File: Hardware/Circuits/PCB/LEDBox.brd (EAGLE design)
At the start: 28 x 28 mm, 19 parts

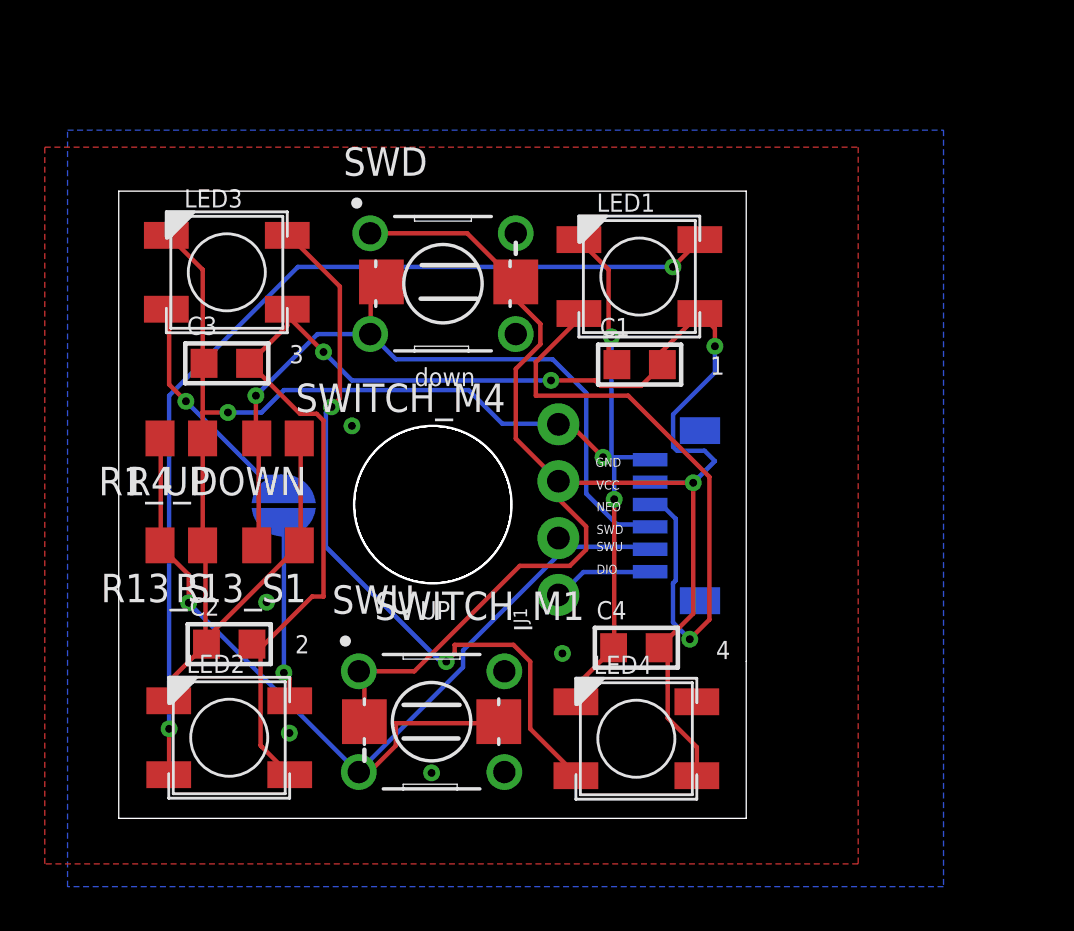
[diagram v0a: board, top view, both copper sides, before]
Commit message: enable Motor
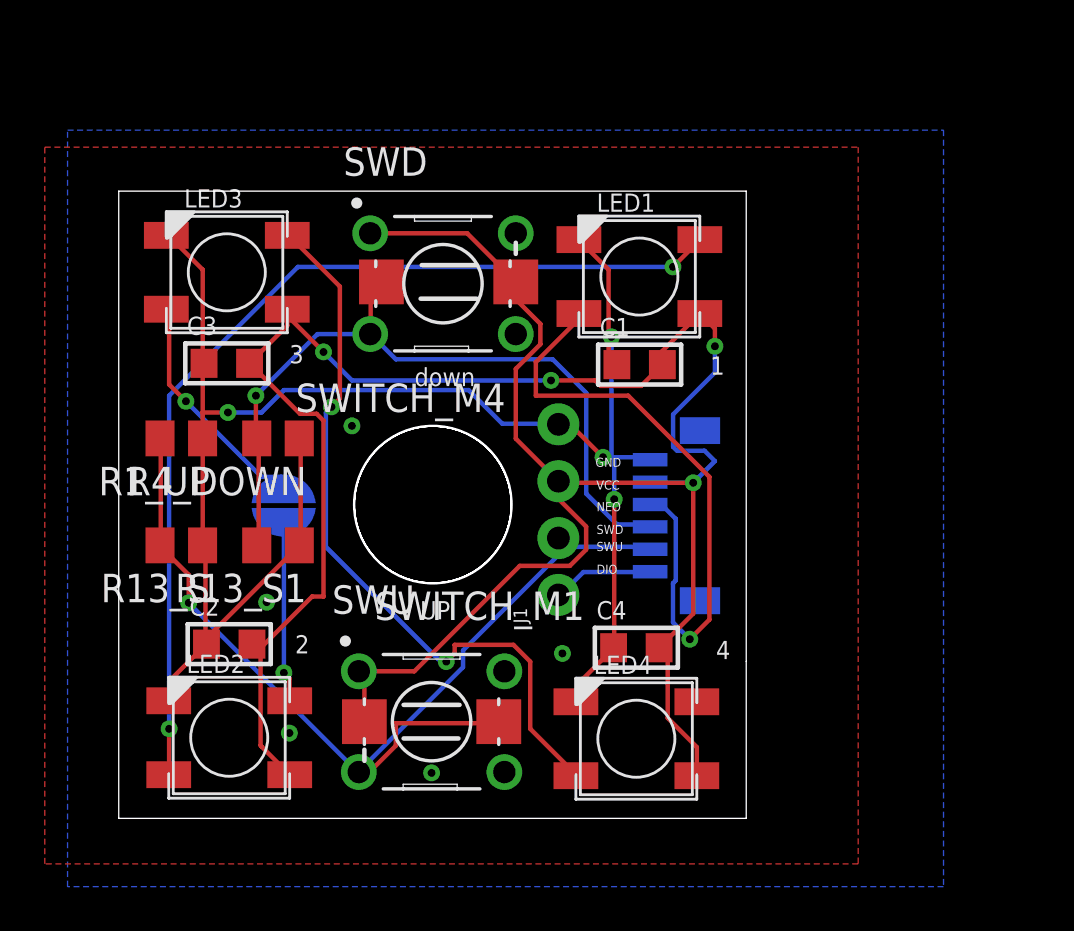
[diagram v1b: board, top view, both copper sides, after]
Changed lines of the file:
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@@
 <?xml version="1.0" encoding="utf-8"?>
 <!DOCTYPE eagle SYSTEM "eagle.dtd">
-<eagle version="9.5.2">
+<eagle version="9.6.2">
 <drawing>
 <settings>
-<setting alwaysvectorfont="no"/>
+<setting alwaysvectorfont="yes"/>
 <setting verticaltext="up"/>
 </settings>
@@
 </layers>
 <board>
-<fusionsync huburn="a.cGVyc29uYWw6dWUyYmFkZWI5" projecturn="a.cGVyc29uYWw6dWUyYmFkZWI5IzIwMTkwNzI5MjA1OTgzMzU2" f3durn="urn:adsk.wipprod:dm.lineage:mkGb1imxSbqdn5AGzfcxTg" pcbguid="4129be0b-5349-4aed-8831-2b5f8f2916f7" lastpulledtime="" lastsyncedchangeguid="7d1ffd36-9ad2-5190-24a6-9f90e3f6ed93"/>
+<fusionsync huburn="a.cGVyc29uYWw6dWUyYmFkZWI5" projecturn="a.cGVyc29uYWw6dWUyYmFkZWI5IzIwMTkwNzI5MjA1OTgzMzU2" f3durn="urn:adsk.wipprod:dm.lineage:mkGb1imxSbqdn5AGzfcxTg" pcbguid="4129be0b-5349-4aed-8831-2b5f8f2916f7" lastpulledtime="2020-11-12T00:39:24Z" lastsyncedchangeguid="3cea0237-b394-707a-1cef-9979548a3917" latestrevisionid="" lastsyncedrevisionid="" lastboardhashguid="3cea0237-b394-707a-1cef-9979548a3917" lastpushedtime="2020-11-12T00:31:10Z" linktopcb3d="false"/>
 <fusionteam huburn="a.cGVyc29uYWw6dWUyYmFkZWI5" projecturn="a.cGVyc29uYWw6dWUyYmFkZWI5IzIwMTkwNzI5MjA1OTgzMzU2" folderUrn="urn:adsk.wipprod:fs.folder:co.fyRBnQNXQZ2K2Ph0YUv8vg" urn="urn:adsk.wipprod:dm.lineage:N41nUebqTaO0nGd6K4BbkA"  versionUrn="urn:adsk.wipprod:fs.file:vf.N41nUebqTaO0nGd6K4BbkA?version=3" camFileUrn="" camFileVersionUrn="" lastpublishedchangeguid="acd2ba34-f1b5-65f4-59b4-86d853f093b3"/>
 <plain>
 <text x="21.326" y="14.682" size="0.4064" layer="21">VCC</text>
 <text x="21.286" y="15.698" size="0.4064" layer="21">GND</text>
-<circle x="14.02563125" y="14.011040625" radius="3.5" width="0.01" layer="20"/>
-<circle x="14.02563125" y="14.011040625" radius="3.5" width="0.01" layer="20"/>
-<circle x="14.02563125" y="14.011040625" radius="3.5" width="0.01" layer="20"/>
-<wire x1="28.021" y1="28.009" x2="28.021" y2="7.009" width="0.01" layer="20"/>
-<wire x1="28.021" y1="0" x2="28.021" y2="7.009" width="0.01" layer="20"/>
-<wire x1="0" y1="28.009" x2="0" y2="0" width="0.01" layer="20"/>
-<wire x1="0" y1="0" x2="28.021" y2="0" width="0.01" layer="20"/>
-<circle x="14.02563125" y="14.011040625" radius="3.54" width="0.01" layer="20"/>
-<wire x1="28.021" y1="28.009" x2="0" y2="28.009" width="0.01" layer="20"/>
 <circle x="14.00171875" y="5.259" radius="1.75" width="0.01" layer="22"/>
 <text x="13.208" y="19.304" size="0.8128" layer="21">down</text>
@@
 <text x="21.336" y="10.922" size="0.4064" layer="21">DIO</text>
 <text x="13.462" y="8.89" size="0.8128" layer="21">UP</text>
+<wire x1="28.021" y1="28.009" x2="28.021" y2="7.009" width="0.01" layer="20"/>
+<wire x1="28.021" y1="7.009" x2="28.021" y2="0" width="0.01" layer="20"/>
+<wire x1="28.021" y1="0" x2="0" y2="0" width="0.01" layer="20"/>
+<wire x1="0" y1="0" x2="0" y2="28.009" width="0.01" layer="20"/>
+<wire x1="0" y1="28.009" x2="28.021" y2="28.009" width="0.01" layer="20"/>
+<circle x="14.026" y="14.011" radius="3.5" width="0.01" layer="20"/>
+<circle x="14.026" y="14.011" radius="3.5" width="0.01" layer="20"/>
+<circle x="14.026" y="14.011" radius="3.5" width="0.01" layer="20"/>
+<circle x="14.026" y="14.011" radius="3.54" width="0.01" layer="20"/>
 </plain>
 <attributes>
@@
 <wire x1="22" y1="7.5" x2="22.098" y2="7.62" width="0.2" layer="1"/>
 <wire x1="20.5" y1="5.25" x2="20.414" y2="5.206" width="0.2" layer="1"/>
-<wire x1="21.625" y1="16.125" x2="22" y2="16.125" width="0.2" layer="16"/>
 <wire x1="22" y1="16.125" x2="22.125" y2="16.125" width="0.2" layer="16"/>
 <wire x1="22.125" y1="16.125" x2="23.625" y2="16.125" width="0.2" layer="16"/>
@@
 <via x="7.62" y="3.81" extent="1-16" drill="0.35"/>
 <via x="13.97" y="2.032" extent="1-16" drill="0.35"/>
+<wire x1="8.062" y1="16.967" x2="10.414" y2="17.526" width="0" layer="19" extent="1-1"/>
+<wire x1="19.812" y1="7.366" x2="20.414" y2="5.206" width="0" layer="19" extent="1-1"/>
+<wire x1="6.604" y1="9.652" x2="8.062" y2="12.192" width="0" layer="19" extent="1-1"/>
+<wire x1="7.62" y1="3.81" x2="3.918" y2="7.78" width="0" layer="19" extent="1-1"/>
+<wire x1="13.97" y1="2.032" x2="7.62" y2="3.81" width="0" layer="19" extent="1-1"/>
 </signal>
 <signal name="VCC">
@@
 </signals>
 <mfgpreviewcolors>
-<mfgpreviewcolor name="soldermaskcolor" color="0xC8008000"/>
-<mfgpreviewcolor name="silkscreencolor" color="0xFFFEFEFE"/>
+<mfgpreviewcolor name="soldermaskcolor" color="0xC8FFFFFF"/>
+<mfgpreviewcolor name="silkscreencolor" color="0xFF000000"/>
 <mfgpreviewcolor name="backgroundcolor" color="0xFF282828"/>
 <mfgpreviewcolor name="coppercolor" color="0xFFFFBF00"/>

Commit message: update circuits
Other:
- outline, holes or cut-outs redrawn
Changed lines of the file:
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@@
 <drawing>
 <settings>
-<setting alwaysvectorfont="yes"/>
+<setting alwaysvectorfont="no"/>
 <setting verticaltext="up"/>
 </settings>
 <grid distance="10" unitdist="mil" unit="mm" style="lines" multiple="1" display="no" altdistance="1" altunitdist="mil" altunit="mm"/>
 <layers>
-<layer number="1" name="Top" color="4" fill="1" visible="yes" active="yes"/>
+<layer number="1" name="Top" color="4" fill="1" visible="no" active="yes"/>
 <layer number="2" name="Route2" color="16" fill="1" visible="no" active="no"/>
 <layer number="3" name="Route3" color="17" fill="1" visible="no" active="no"/>
@@
 <layer number="14" name="Route14" color="22" fill="1" visible="no" active="no"/>
 <layer number="15" name="Route15" color="23" fill="1" visible="no" active="no"/>
-<layer number="16" name="Bottom" color="1" fill="1" visible="yes" active="yes"/>
+<layer number="16" name="Bottom" color="1" fill="1" visible="no" active="yes"/>
 <layer number="17" name="Pads" color="2" fill="1" visible="yes" active="yes"/>
-<layer number="18" name="Vias" color="2" fill="1" visible="yes" active="yes"/>
-<layer number="19" name="Unrouted" color="6" fill="1" visible="yes" active="yes"/>
+<layer number="18" name="Vias" color="2" fill="1" visible="no" active="yes"/>
+<layer number="19" name="Unrouted" color="6" fill="1" visible="no" active="yes"/>
 <layer number="20" name="Dimension" color="24" fill="1" visible="yes" active="yes"/>
-<layer number="21" name="tPlace" color="7" fill="1" visible="yes" active="yes"/>
+<layer number="21" name="tPlace" color="7" fill="1" visible="no" active="yes"/>
 <layer number="22" name="bPlace" color="7" fill="1" visible="yes" active="yes"/>
-<layer number="23" name="tOrigins" color="15" fill="1" visible="yes" active="yes"/>
-<layer number="24" name="bOrigins" color="15" fill="1" visible="yes" active="yes"/>
-<layer number="25" name="tNames" color="7" fill="1" visible="yes" active="yes"/>
-<layer number="26" name="bNames" color="7" fill="1" visible="yes" active="yes"/>
+<layer number="23" name="tOrigins" color="15" fill="1" visible="no" active="yes"/>
+<layer number="24" name="bOrigins" color="15" fill="1" visible="no" active="yes"/>
+<layer number="25" name="tNames" color="7" fill="1" visible="no" active="yes"/>
+<layer number="26" name="bNames" color="7" fill="1" visible="no" active="yes"/>
 <layer number="27" name="tValues" color="7" fill="1" visible="no" active="yes"/>
 <layer number="28" name="bValues" color="7" fill="1" visible="no" active="yes"/>
@@
 <layer number="43" name="vRestrict" color="2" fill="10" visible="no" active="yes"/>
 <layer number="44" name="Drills" color="7" fill="1" visible="no" active="yes"/>
-<layer number="45" name="Holes" color="7" fill="1" visible="no" active="yes"/>
+<layer number="45" name="Holes" color="7" fill="1" visible="yes" active="yes"/>
 <layer number="46" name="Milling" color="3" fill="1" visible="no" active="yes"/>
 <layer number="47" name="Measures" color="7" fill="1" visible="no" active="yes"/>
-<layer number="48" name="Document" color="7" fill="1" visible="no" active="yes"/>
+<layer number="48" name="Document" color="7" fill="1" visible="yes" active="yes"/>
 <layer number="49" name="Reference" color="7" fill="1" visible="no" active="yes"/>
 <layer number="50" name="dxf" color="7" fill="1" visible="no" active="no"/>
@@
 <text x="21.336" y="10.922" size="0.4064" layer="21">DIO</text>
 <text x="13.462" y="8.89" size="0.8128" layer="21">UP</text>
-<wire x1="28.021" y1="28.009" x2="28.021" y2="7.009" width="0.01" layer="20"/>
-<wire x1="28.021" y1="7.009" x2="28.021" y2="0" width="0.01" layer="20"/>
+<wire x1="28.021" y1="28.009" x2="28.021" y2="0" width="0.01" layer="20"/>
 <wire x1="28.021" y1="0" x2="0" y2="0" width="0.01" layer="20"/>
 <wire x1="0" y1="0" x2="0" y2="28.009" width="0.01" layer="20"/>
@@
 <circle x="14.026" y="14.011" radius="3.5" width="0.01" layer="20"/>
 <circle x="14.026" y="14.011" radius="3.54" width="0.01" layer="20"/>
+<circle x="19.5834" y="17.5768" radius="0.915809375" width="0.001" layer="48"/>
+<circle x="19.5834" y="15.0368" radius="0.915809375" width="0.001" layer="48"/>
+<circle x="19.5834" y="12.4968" radius="0.915809375" width="0.001" layer="48"/>
+<circle x="19.5834" y="9.9568" radius="0.915809375" width="0.001" layer="48"/>
 </plain>
 <attributes>

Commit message: update motors
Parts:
- removed R13_S, R13_S1, R1_UP: 10K, resistor:M0805
- removed SWD, SWU: B3F-1000, Switch:B3F-1000
- removed SWITCH_M1: DTSM-3, switch-tact:DTSM-3
- added C5: 0.1uF, SparkFun-Capacitors:0603
- added R4_DOWN1: 10k, SparkFun-Resistors:0603
- added U1: TEXAS_INSTRUMENTS_DRV5033FAQDBZRTEXAS_INSTRUMENTS_DRV5033FA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, Texas Instruments - DRV5033FAQDBZR:TEXAS_INSTRUMENTS_DRV5033FAQDBZR_0
- C1, C2, C3, C4: value 0.1uf -> 0.1uF; device rc-master-smd:C0805 -> SparkFun-Capacitors:0603
- JP1: value JUMPER-SMT_2_NO_NO-SILK_ROUND -> LED; device SparkFun-Jumpers:SMT-JUMPER_2_NO_NO-SILK_ROUND -> SparkFun-Jumpers:SMT-JUMPER_2_NC_TRACE_NO-SILK
- R4_DOWN: value 10K -> 10k; device resistor:M0805 -> SparkFun-Resistors:0603
- moved LED2 26.3 mm to (9.00, 29.6)
- moved LED3 17.5 mm to (9.00, 7.37)
- moved R4_DOWN 13.3 mm to (18.1, 24.4), turned to 0 degrees
- moved LED1 7.15 mm to (27.9, 29.6)
- moved SWITCH_M4 6.81 mm to (18.3, 29.8), turned to 0 degrees
- moved J2 6.65 mm to (29.8, 18.0)
- moved C4 6.38 mm to (27.4, 12.3)
- moved C1 6.38 mm to (27.8, 24.7)
- moved JP1 6.35 mm to (11.2, 19.1), flipped to the top, turned to 270 degrees
- moved LED4 6.15 mm to (27.9, 7.37)
- moved J1 5.66 mm to (23.8, 13.8)
- moved C3 5.24 mm to (6.86, 25.1)
- moved C2 5.07 mm to (6.84, 12.5)
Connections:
- net GND: now also C5.1, U1.3; no longer R13_S.1, R13_S1.1, R1_UP.1
- net SWD_IN: no longer R13_S1.2, SWD.3
- net SWU_IN: now also R4_DOWN1.2, U1.2; no longer R13_S.2, R1_UP.2, SWITCH_M1.2, SWU.3
- net VCC: now also C5.2, R4_DOWN1.1, U1.1; no longer SWD.1, SWITCH_M1.1, SWU.1
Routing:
- net SWU_IN: track 45.1 -> 15.6 mm, vias 1 -> 0
- net N$6: track 33.2 -> 15.4 mm, vias 2 -> 0
- net N$1: track 43.5 -> 27.5 mm, vias 2 -> 0
- net NEO_IN: track 28.5 -> 13.4 mm
- net GND: track 78.4 -> 65.3 mm, vias 9 -> 1
- net SWD_IN: track 34.3 -> 21.8 mm
- net VCC: track 116.7 -> 127.8 mm, vias 4 -> 6
- net N$2: track 7.56 -> 14.7 mm, vias 1 -> 2
- net N$4: track 10.2 -> 15.9 mm, vias 1 -> 0
- net DIO_IN: track 4.52 -> 5.48 mm
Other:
- board size 28 x 28 mm -> 29.5 x 29.5 mm
- board text added: "+"
- board text added: "-"
- board text added: "DOWN"
- board text removed: "1"
- board text removed: "2"
- board text removed: "3"
- board text removed: "4"
- board text removed: "SWD"
- board text removed: "down"
